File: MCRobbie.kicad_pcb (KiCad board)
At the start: 2 copper layers, 8 parts, among them J0 Motor0, J1 Motor1, J2 Motor2, J3 Motor3, J4 I2C_Header, J5 ICP_Header, J6 Power_Header

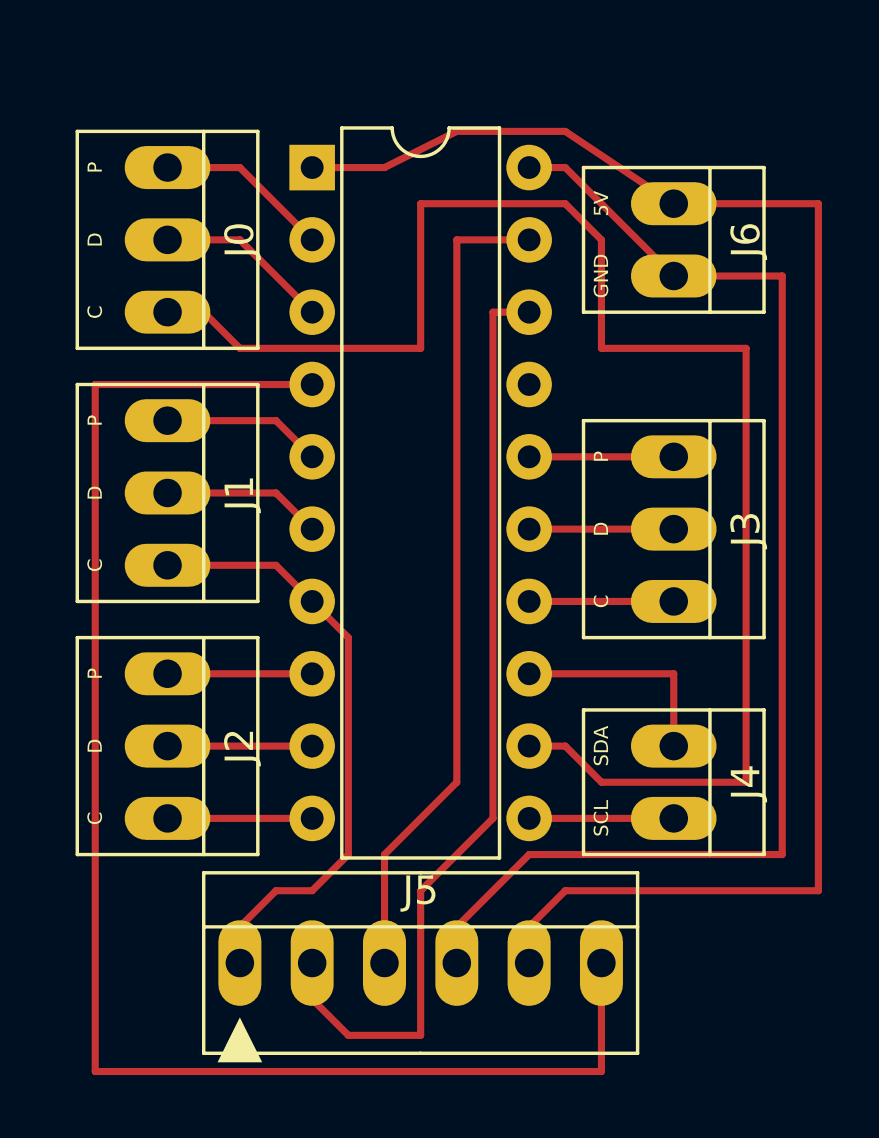
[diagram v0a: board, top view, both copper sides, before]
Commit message: Added pcb and schematic to repo
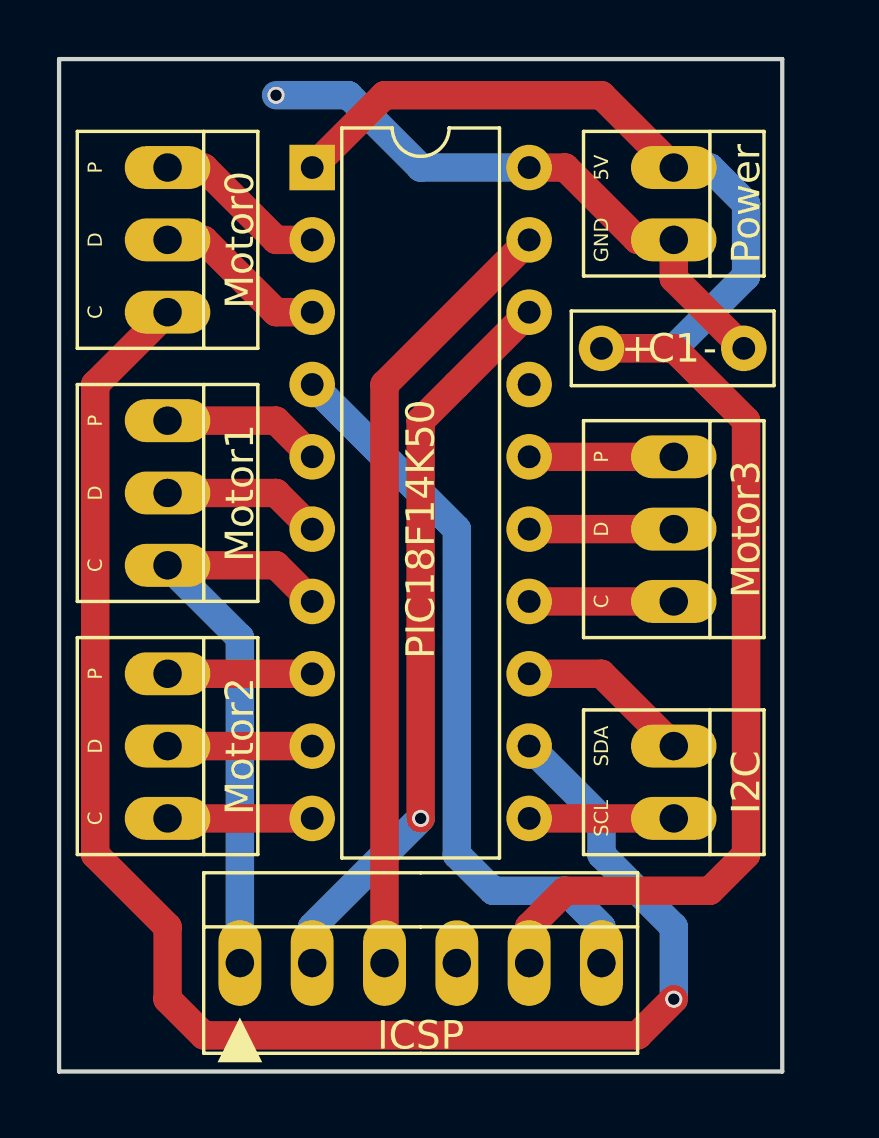
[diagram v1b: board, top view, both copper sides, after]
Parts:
- removed ?: PIC18F14K50, Housings_DIP:DIP-20_W7.62mm
- removed J0: Motor0, Connectors:PINHEAD1-3
- removed J1: Motor1, Connectors:PINHEAD1-3
- removed J2: Motor2, Connectors:PINHEAD1-3
- removed J3: Motor3, Connectors:PINHEAD1-3
- removed J4: I2C_Header, Connectors:PINHEAD1-2
- removed J5: ICP_Header, Connectors:PINHEAD1-6
- removed J6: Power_Header, Connectors:PINHEAD1-2
- added C1: , Capacitors_THT:C_Rect_L7.0mm_W2.5mm_P5.00mm, F.Cu at (151.1, 96.5)
- added I2C: I2C_Header, Connectors:PINHEAD1-2, F.Cu at (153.7, 110.5)
- added ICSP: ICP_Header, Connectors:PINHEAD1-6, F.Cu at (138.4, 118.1)
- added Motor0: Motor0, Connectors:PINHEAD1-3, F.Cu at (135.9, 90.2)
- added Motor1: Motor1, Connectors:PINHEAD1-3, F.Cu at (135.9, 99.1)
- added Motor2: Motor2, Connectors:PINHEAD1-3, F.Cu at (135.9, 108.0)
- added Motor3: Motor3, Connectors:PINHEAD1-3, F.Cu at (153.7, 100.3)
- added PIC18F14K50: PIC18F14K50, Housings_DIP:DIP-20_W7.62mm, F.Cu at (141.0, 90.2)
- added Power: Power_Header, Connectors:PINHEAD1-2, F.Cu at (153.7, 90.2)
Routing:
- net Net-(J5-Pad6): track 53.3 -> 26.0 mm
- net GND: track 44.5 -> 20.9 mm, vias 0 -> 1
- net Net-(J5-Pad2): track 33.3 -> 26.0 mm, vias 0 -> 1
- net +5V: track 54.9 -> 57.9 mm
- net Net-(J0-Pad3): track 53.6 -> 56.1 mm, vias 0 -> 1
- net Net-(J5-Pad3): track 29.0 -> 27.5 mm
- net Net-(J4-Pad1): track 7.62 -> 6.13 mm
- net Net-(J1-Pad1): track 6.88 -> 5.61 mm
- net Net-(J1-Pad3): track 21.2 -> 20.6 mm
- added copper zone on B.Cu, net GND
- added copper zone on F.Cu, net GND
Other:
- board outline added: 25.4 x 35.6 mm
- net class Default: trace_width 0.25 -> 1
- board text added: "+"
- board text added: "-"
- board text added: "Copyright OokTech CC-BY-SA"
- board text added: "Design by OokTech"
- board text added: "MCRobbie v.1.0.1 2017"
- board text removed: "MCRobbie v.1 2017 Designed by OokTech"
